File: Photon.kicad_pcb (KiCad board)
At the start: 2 copper layers, 21.2 x 74.4 mm, 53 parts, among them J1 USB_C_Receptacle_USB2.0_14P, Q1 IRLML6402, Q2 IRLML6402, SW1 TS-1088-AR02016, U1 ATtiny13A-S, U2 RT8059GJ5, U3 TP4056, U4 BCR421UW6-7, U5 DW01A, U6 FS8205A, U7 BCR421UW6-7

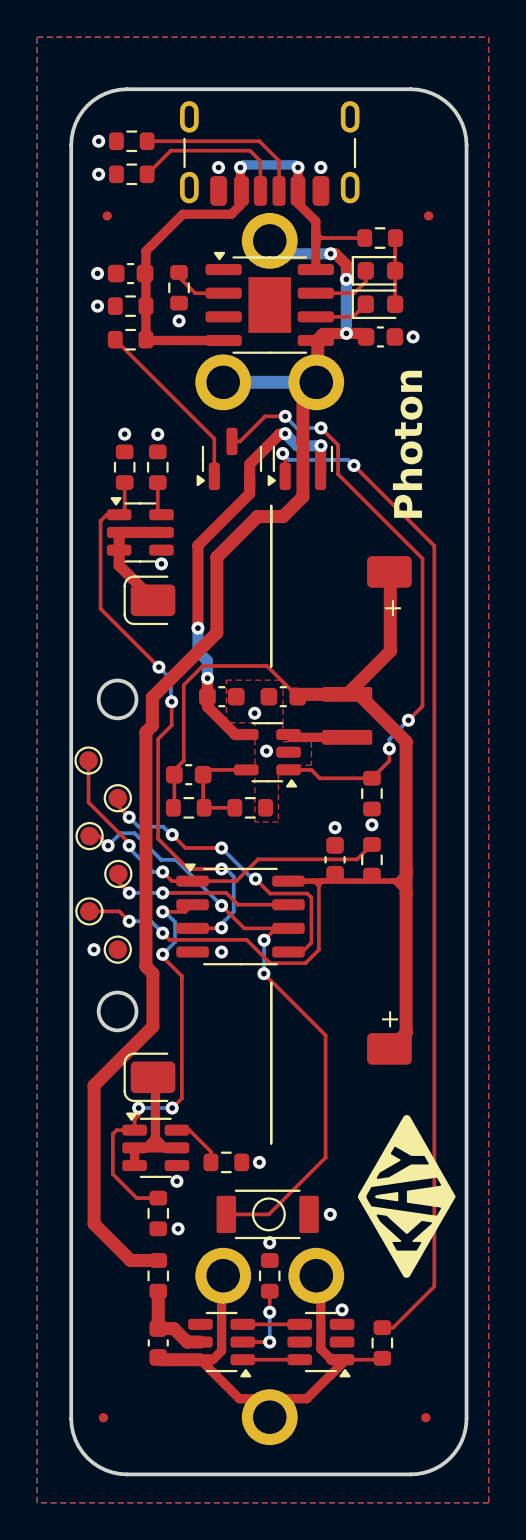
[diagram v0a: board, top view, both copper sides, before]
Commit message: Updated schem and PCB. updated footprints
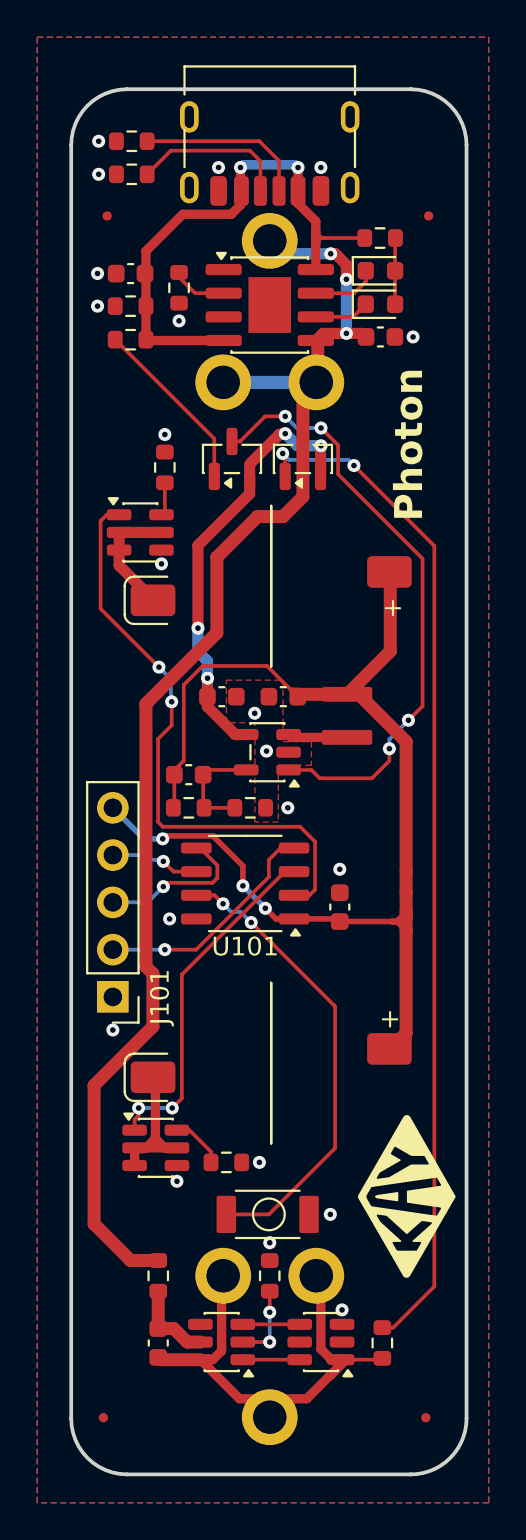
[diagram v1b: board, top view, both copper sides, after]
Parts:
- removed R12, R15, R6: 100K, Resistor_SMD:R_0603_1608Metric
- removed R18: 10K, Resistor_SMD:R_0603_1608Metric
- removed TP1: GND, TestPoint:TestPoint_Pad_D1.0mm
- removed TP12: SCK, TestPoint:TestPoint_Pad_D1.0mm
- removed TP13: RESET, TestPoint:TestPoint_Pad_D1.0mm
- removed TP7: MOSI, TestPoint:TestPoint_Pad_D1.0mm
- removed TP8: MISO, TestPoint:TestPoint_Pad_D1.0mm
- removed TP9: 3V3, TestPoint:TestPoint_Pad_D1.0mm
- removed U1: ATtiny13A-S, Package_SO:SO-8_3.9x4.9mm_P1.27mm
- added J101: Conn_01x05_Socket, Connector_PinHeader_2.54mm:PinHeader_1x05_P2.54mm_Vertical, F.Cu at (44.5, 69.1)
- added U101: PY32F002AL15S6TU, Package_SO:SOP-8_3.9x4.9mm_P1.27mm, F.Cu at (51.6, 63.0)
- C1: value 4.7uF -> 100nF
- C2: value 4.7uF -> 10uF
- C7: value 0.1uF -> 100nF
- moved C1 2.55 mm to (56.6, 64.3)
- moved R13 0.38 mm to (47.2, 40.6)
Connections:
- SW1 pad 1: /MISO_BTN -> /BTN
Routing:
- net /MISO_BTN: track 34.6 -> 0.00 mm, vias 4 -> 0
- net /BTN: track 0.00 -> 24.9 mm, vias 0 -> 2
- net /RESET: track 20.3 -> 0.00 mm, vias 2 -> 0
- net /MOSI: track 16.7 -> 0.00 mm, vias 4 -> 0
- net /SWC: track 0.00 -> 12.5 mm, vias 0 -> 1
- net /SCK: track 10.1 -> 0.00 mm, vias 2 -> 0
- net /SWD: track 0.00 -> 8.35 mm, vias 0 -> 1
- net +3V3: track 71.6 -> 66.2 mm, vias 2 -> 3
- net /NRST: track 0.00 -> 4.86 mm, vias 0 -> 1
- net /LED2_EN: track 23.2 -> 19.0 mm, vias 4 -> 2
- net /LED1_EN: track 31.6 -> 31.9 mm, vias 4 -> 2
- net GND: vias 23 -> 21
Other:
- outline, holes or cut-outs redrawn
- rule pad_to_mask_clearance: 0.1 -> 0
- rule solder_mask_min_width: 0.2 -> 0.1

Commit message: added stitching vias and bi direction led for charging
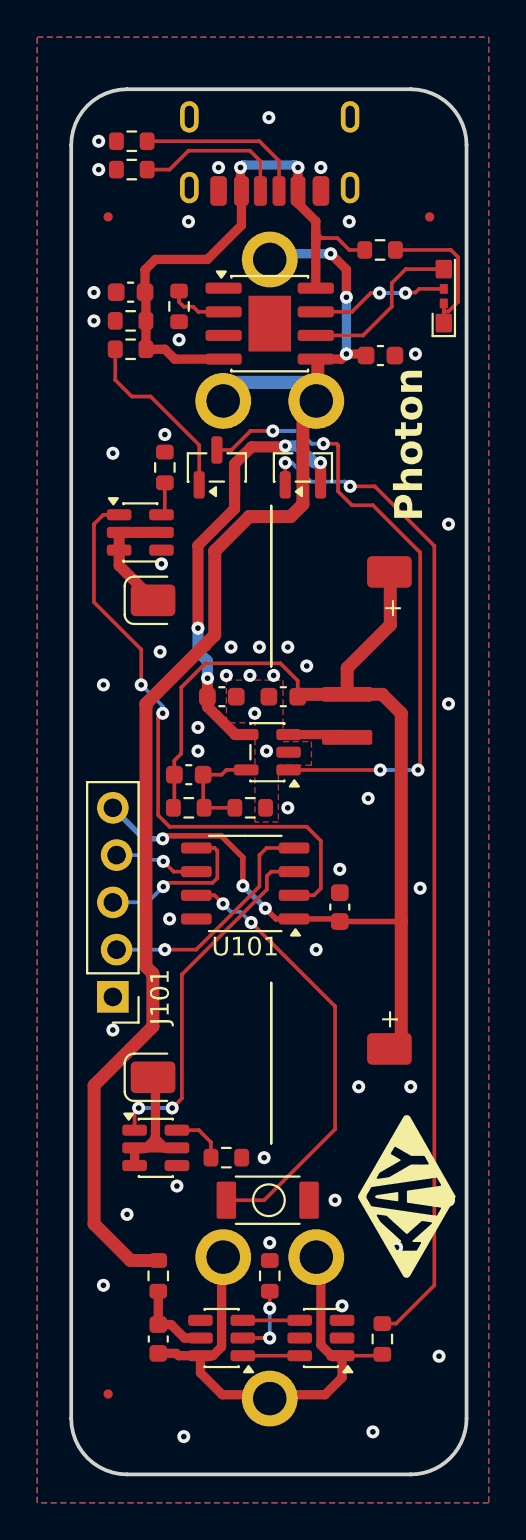
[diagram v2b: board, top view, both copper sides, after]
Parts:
- removed D2: SZYY0603R1, LED_SMD:LED_0603_1608Metric
- removed the FID2 at (61.3, 91.7)
- D1: value SZYY0603R1 -> LED_Dual_AKAK; footprint LED_SMD:LED_0603_1608Metric -> Photon:3.9mm Bi directional side mount LED
- moved G*** 6.27 mm to (58.2, 47.8)
- moved D1 3.89 mm to (62.2, 30.0), turned to -90 degrees
- moved FID2 1.30 mm to (44.2, 90.4)
- moved C3 1.00 mm to (45.4, 31.2)
- moved C6 1.00 mm to (58.8, 34.6)
- moved R10 1.00 mm to (48.0, 32.0)
- moved U3 1.00 mm to (52.9, 32.9)
- moved Q1 0.93 mm to (50.0, 40.6)
- moved R5 0.79 mm to (45.4, 32.8)
- moved SW1 0.76 mm to (52.8, 80.0)
- moved R7 0.64 mm to (58.8, 29.0)
- moved R4 0.51 mm to (45.4, 34.3)
- moved Q2 0.46 mm to (54.7, 40.6)
- moved R2 0.25 mm to (45.5, 24.6)
- moved R16 0.25 mm to (50.5, 77.7)
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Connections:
- D1 pad 1: /STAT2 -> /LED_PWR
- D1 pad 2: /LED_PWR -> /STAT1
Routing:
- net /STAT2: track 2.97 -> 9.10 mm
- net /LED_PWR: track 3.28 -> 7.96 mm
- net /STAT1: track 3.53 -> 7.39 mm, vias 0 -> 2
- net 5V: track 30.5 -> 32.2 mm
- net /BUCK_EN: track 32.5 -> 34.2 mm
- net /Bat+: track 74.2 -> 75.5 mm
- net +3V3: track 66.2 -> 65.0 mm
- net /Bat-: track 25.0 -> 25.9 mm
- net /BTN: track 24.9 -> 23.9 mm
- net /DSBL: track 9.90 -> 9.26 mm
- net /BAT_DSBL: track 55.0 -> 54.4 mm
- net GND: vias 21 -> 50
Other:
- board text added: "Built In Toronto, Canada"
- board text added: "V5"
- board text removed: "V4"

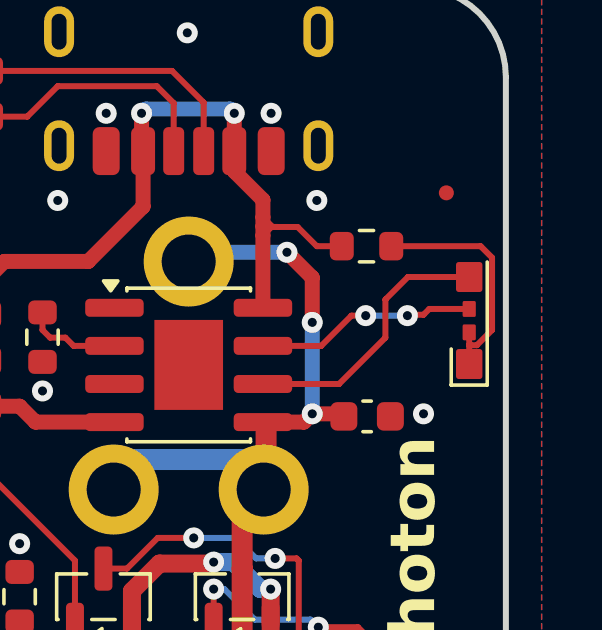
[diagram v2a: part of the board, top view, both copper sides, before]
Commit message: Edged clearance resolved and programming connector modified
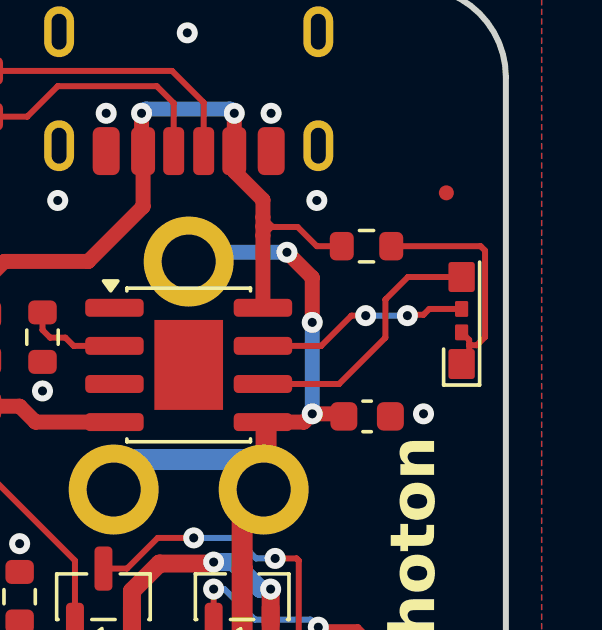
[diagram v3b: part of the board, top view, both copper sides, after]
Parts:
- moved D1 0.25 mm to (62.0, 30.0)

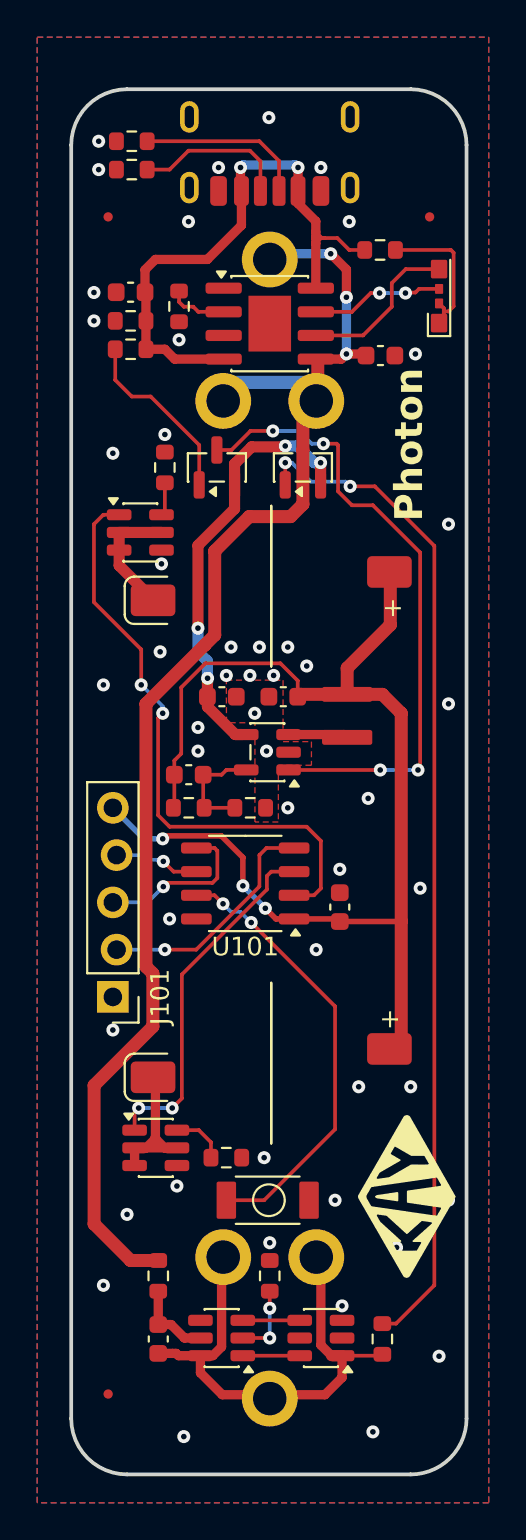
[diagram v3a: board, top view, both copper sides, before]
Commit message: improvements
- added pull down to buck (previously there and was removed)
- Simplified PCB by rotating components to reduce vias
- updated value fields and annotated schematic
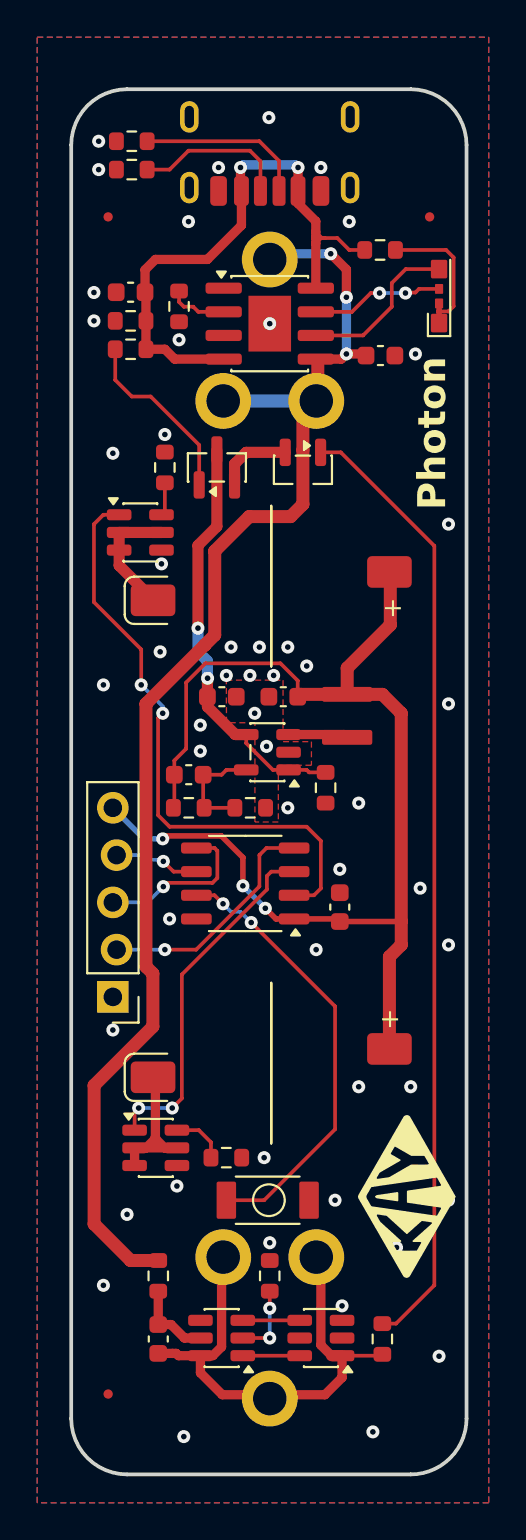
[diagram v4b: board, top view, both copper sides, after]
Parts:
- added R6: 100K, Resistor_SMD:R_0603_1608Metric, F.Cu at (55.9, 57.8)
- R4: value 100R -> 2K
- moved Q2 0.13 mm to (54.7, 40.8), turned to -90 degrees
- renumbered D5 to D2, D6 to D3, J101 to J2, U101 to U1, U3 to U2, U2 to U3
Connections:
- net /Bat+ renamed +BATT
- net /STAT1 renamed /CHRG
- net /STAT2 renamed /STDBY
- C2 pad 2: PACK_SAFE -> /VBAT_SYS
- Q1 pad 3: /BUCK_EN -> /VBAT_SYS
- U2 pad 1: (no net) -> GND
- U2 pad 9: (no net) -> GND
- U3 pad 1: /BUCK_EN -> /VBAT_SYS
- U3 pad 4: PACK_SAFE -> /VBAT_SYS
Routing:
- net /BUCK_EN: track 34.2 -> 0.00 mm, vias 4 -> 0
- net /VBAT_SYS: track 0.00 -> 22.5 mm, vias 0 -> 2
- net PACK_SAFE: track 23.1 -> 4.11 mm, vias 4 -> 0
- net /BAT_DSBL: track 54.4 -> 51.6 mm, vias 2 -> 0
- net GND: vias 50 -> 52

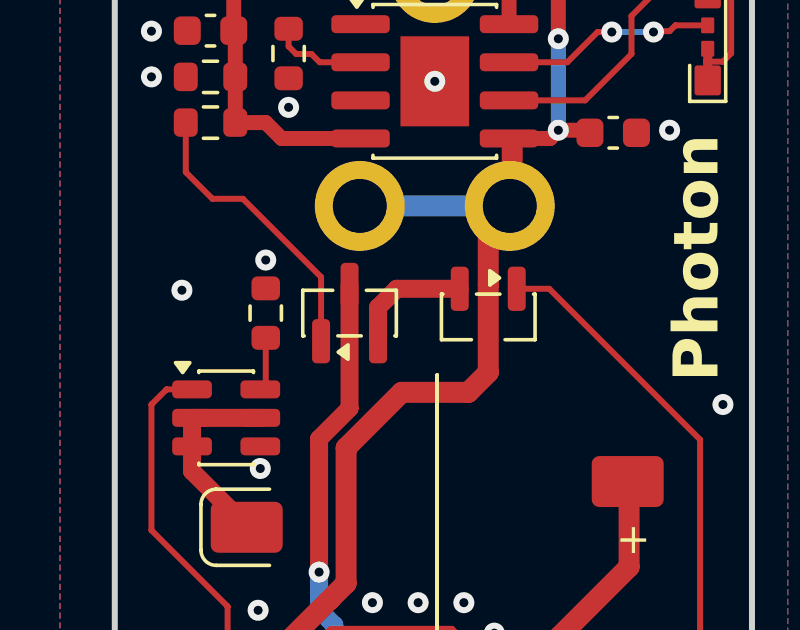
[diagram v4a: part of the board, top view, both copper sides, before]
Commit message: small change
Moved Q1 down .3mm
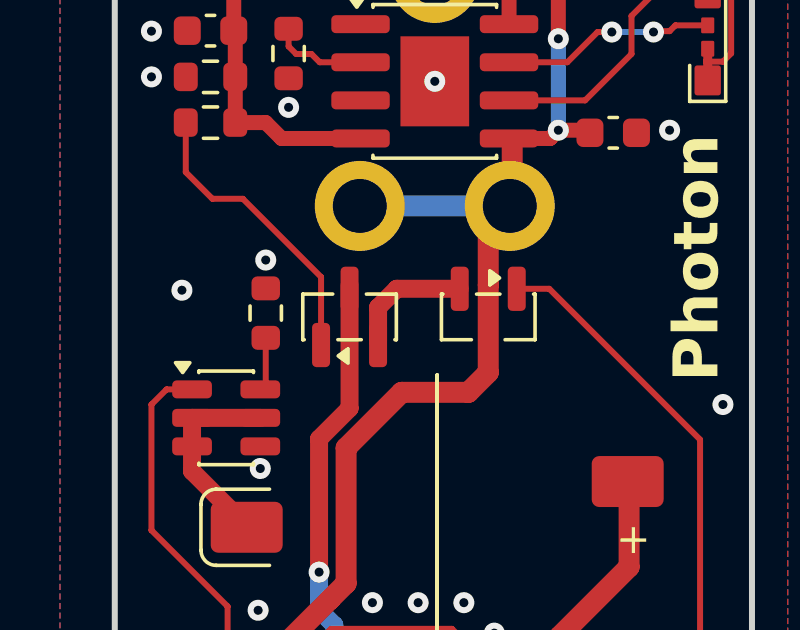
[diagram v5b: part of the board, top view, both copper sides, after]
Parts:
- moved Q1 0.13 mm to (50.0, 40.8)
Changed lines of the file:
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@@
 	(footprint "Package_TO_SOT_SMD:SOT-23"
 		(layer "F.Cu")
-		(at 50.038 40.64 90)
+		(at 50.038 40.767 90)
 		(descr "SOT, 3 Pin (JEDEC TO-236 Var AB https://www.jedec.org/document_search?search_api_views_fulltext=TO-236), generated with kicad-footprint-generator ipc_gullwing_generator.py")
 		(tags "SOT TO_SOT_SMD")

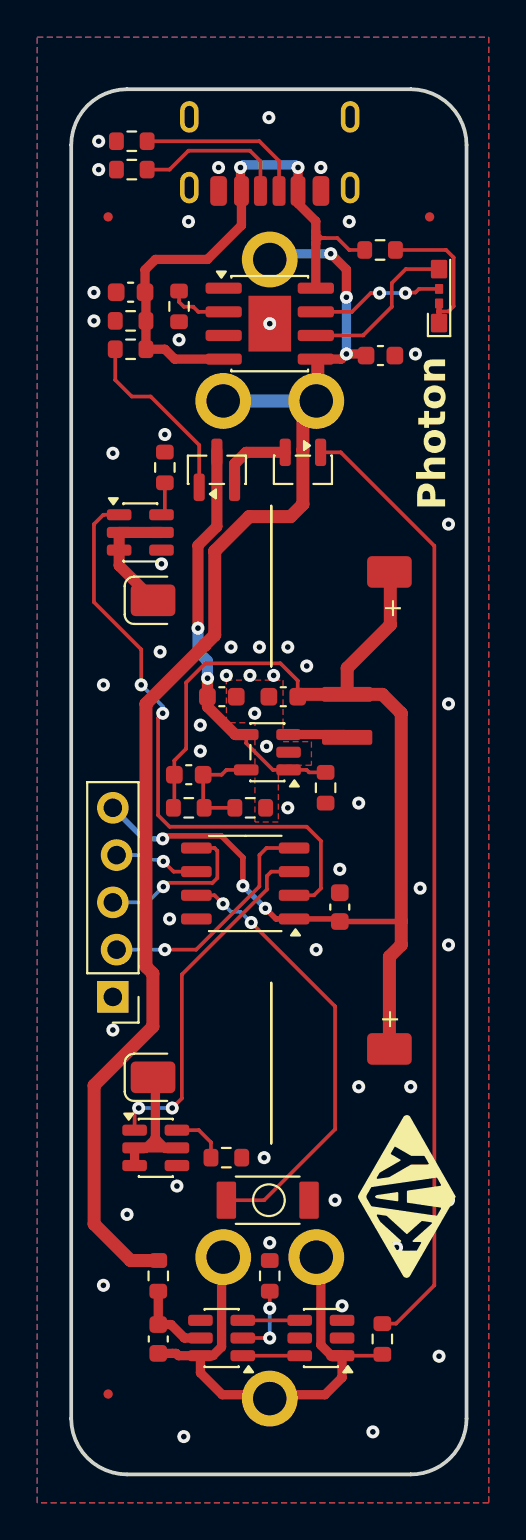
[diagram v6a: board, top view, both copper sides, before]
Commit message: added UVLO for the buck
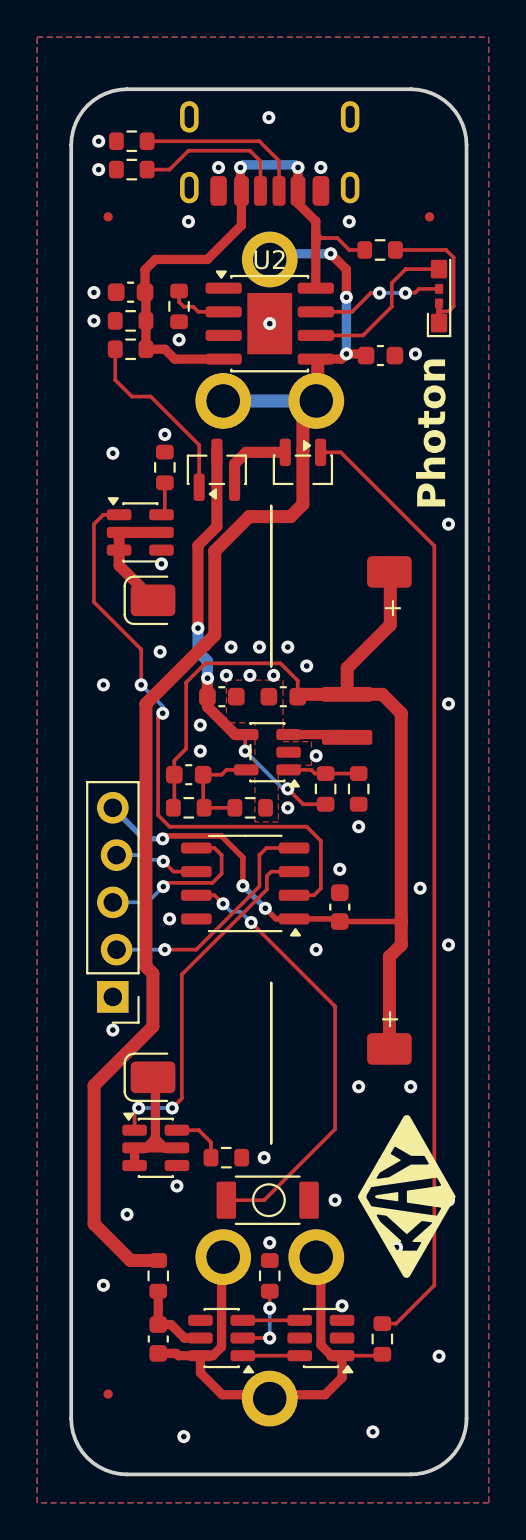
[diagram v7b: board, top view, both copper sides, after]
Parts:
- added R3: 30K, Resistor_SMD:R_0603_1608Metric, F.Cu at (55.9, 57.9)
- U2: footprint Package_SO:SOIC-8-1EP_3.9x4.9mm_P1.27mm_EP2.29x3mm -> Package_SO:SOIC-8-1EP_3.9x4.9mm_P1.27mm_EP2.41x3.3mm
- moved R6 1.78 mm to (57.7, 57.9)
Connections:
- R6 pad 1: /VBAT_SYS -> /UVLO
- U3 pad 1: /VBAT_SYS -> /UVLO
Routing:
- net /UVLO: track 0.00 -> 3.86 mm
- net /VBAT_SYS: track 22.5 -> 23.5 mm, vias 2 -> 4
- net GND: vias 52 -> 51
